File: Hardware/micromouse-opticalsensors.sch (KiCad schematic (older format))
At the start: 18 parts

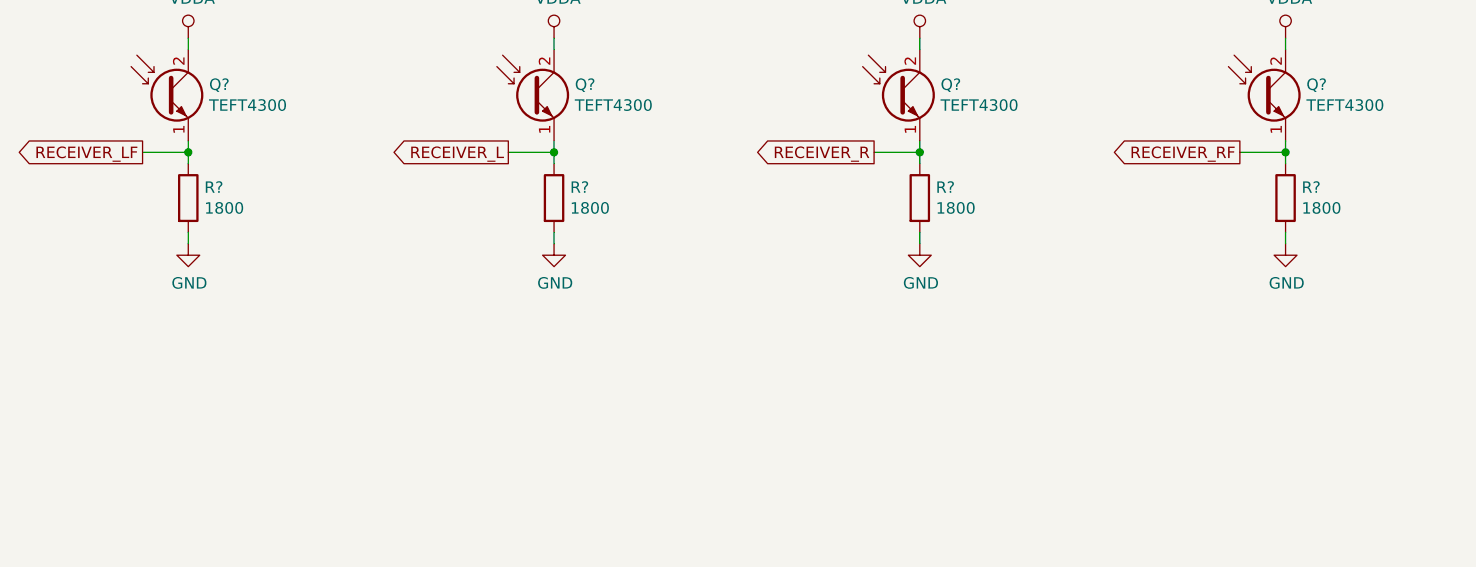
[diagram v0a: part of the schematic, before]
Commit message: add power sub-schematic, fix some supply-connections, rearrange sub-schematics
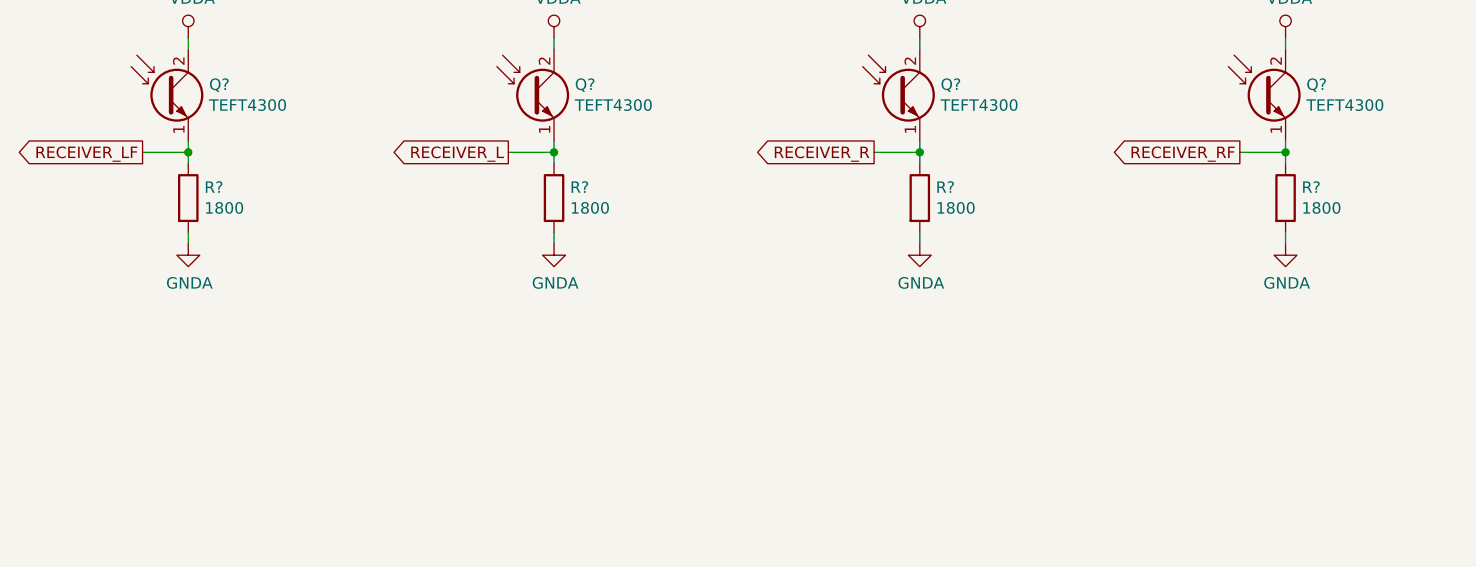
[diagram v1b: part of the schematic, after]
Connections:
- net GND: no longer R?.2, R?.2, R?.2, R?.2
- new net GNDA: R?.2, R?.2, R?.2, R?.2
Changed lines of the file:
@@
 $Descr A4 11693 8268
 encoding utf-8
-Sheet 7 7
+Sheet 7 8
 Title ""
 Date ""
@@
 	1    0    0    -1
 $EndComp
-$Comp
-L power:GND #PWR?
-U 1 1 5C8B70E6
-P 2950 4050
-F 0 "#PWR?" H 2950 3800 50  0001 C CNN
-F 1 "GND" H 2955 3877 50  0000 C CNN
-F 2 "" H 2950 4050 50  0001 C CNN
-F 3 "" H 2950 4050 50  0001 C CNN
-	1    2950 4050
-	1    0    0    -1
-$EndComp
 Wire Wire Line
 	2950 4050 2950 4000
@@
 	1    0    0    -1
 $EndComp
-$Comp
-L power:GND #PWR?
-U 1 1 5C8BA1AA
-P 4550 4050
-F 0 "#PWR?" H 4550 3800 50  0001 C CNN
-F 1 "GND" H 4555 3877 50  0000 C CNN
-F 2 "" H 4550 4050 50  0001 C CNN
-F 3 "" H 4550 4050 50  0001 C CNN
-	1    4550 4050
-	1    0    0    -1
-$EndComp
 Wire Wire Line
 	4550 4050 4550 4000
@@
 	1    0    0    -1
 $EndComp
-$Comp
-L power:GND #PWR?
-U 1 1 5C8BB164
-P 6150 4050
-F 0 "#PWR?" H 6150 3800 50  0001 C CNN
-F 1 "GND" H 6155 3877 50  0000 C CNN
-F 2 "" H 6150 4050 50  0001 C CNN
-F 3 "" H 6150 4050 50  0001 C CNN
-	1    6150 4050
-	1    0    0    -1
-$EndComp
 Wire Wire Line
 	6150 4050 6150 4000
@@
 	1    0    0    -1
 $EndComp
-$Comp
-L power:GND #PWR?
-U 1 1 5C8BB183
+Wire Wire Line
+	7750 4050 7750 4000
+Wire Wire Line
+	7750 3700 7750 3650
+Wire Wire Line
+	7550 3650 7750 3650
+Connection ~ 7750 3650
+Wire Wire Line
+	7750 3650 7750 3600
+$Comp
+L power:GNDA #PWR?
+U 1 1 5C89B1C4
+P 2950 4050
+F 0 "#PWR?" H 2950 3800 50  0001 C CNN
+F 1 "GNDA" H 2955 3877 50  0000 C CNN
+F 2 "" H 2950 4050 50  0001 C CNN
+F 3 "" H 2950 4050 50  0001 C CNN
+	1    2950 4050
+	1    0    0    -1
+$EndComp
+$Comp
+L power:GNDA #PWR?
+U 1 1 5C89EB37
+P 4550 4050
+F 0 "#PWR?" H 4550 3800 50  0001 C CNN
+F 1 "GNDA" H 4555 3877 50  0000 C CNN
+F 2 "" H 4550 4050 50  0001 C CNN
+F 3 "" H 4550 4050 50  0001 C CNN
+	1    4550 4050
+	1    0    0    -1
+$EndComp
+$Comp
+L power:GNDA #PWR?
+U 1 1 5C89EB78
+P 6150 4050
+F 0 "#PWR?" H 6150 3800 50  0001 C CNN
+F 1 "GNDA" H 6155 3877 50  0000 C CNN
+F 2 "" H 6150 4050 50  0001 C CNN
+F 3 "" H 6150 4050 50  0001 C CNN
+	1    6150 4050
+	1    0    0    -1
+$EndComp
+$Comp
+L power:GNDA #PWR?
+U 1 1 5C89EBB9
 P 7750 4050
 F 0 "#PWR?" H 7750 3800 50  0001 C CNN
-F 1 "GND" H 7755 3877 50  0000 C CNN
+F 1 "GNDA" H 7755 3877 50  0000 C CNN
 F 2 "" H 7750 4050 50  0001 C CNN
 F 3 "" H 7750 4050 50  0001 C CNN
@@
 	1    0    0    -1
 $EndComp
-Wire Wire Line
-	7750 4050 7750 4000
-Wire Wire Line
-	7750 3700 7750 3650
-Wire Wire Line
-	7550 3650 7750 3650
-Connection ~ 7750 3650
-Wire Wire Line
-	7750 3650 7750 3600
 $EndSCHEMATC
